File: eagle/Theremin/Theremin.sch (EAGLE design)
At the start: 82 parts, among them Q1 2N3904, Q2 2N3904, Q3 2N3904, Q4 2N3904, Q6 2N3904, Q7 2N3904, Q8 2N3904, U1 LM78L12, U2 LM79L12

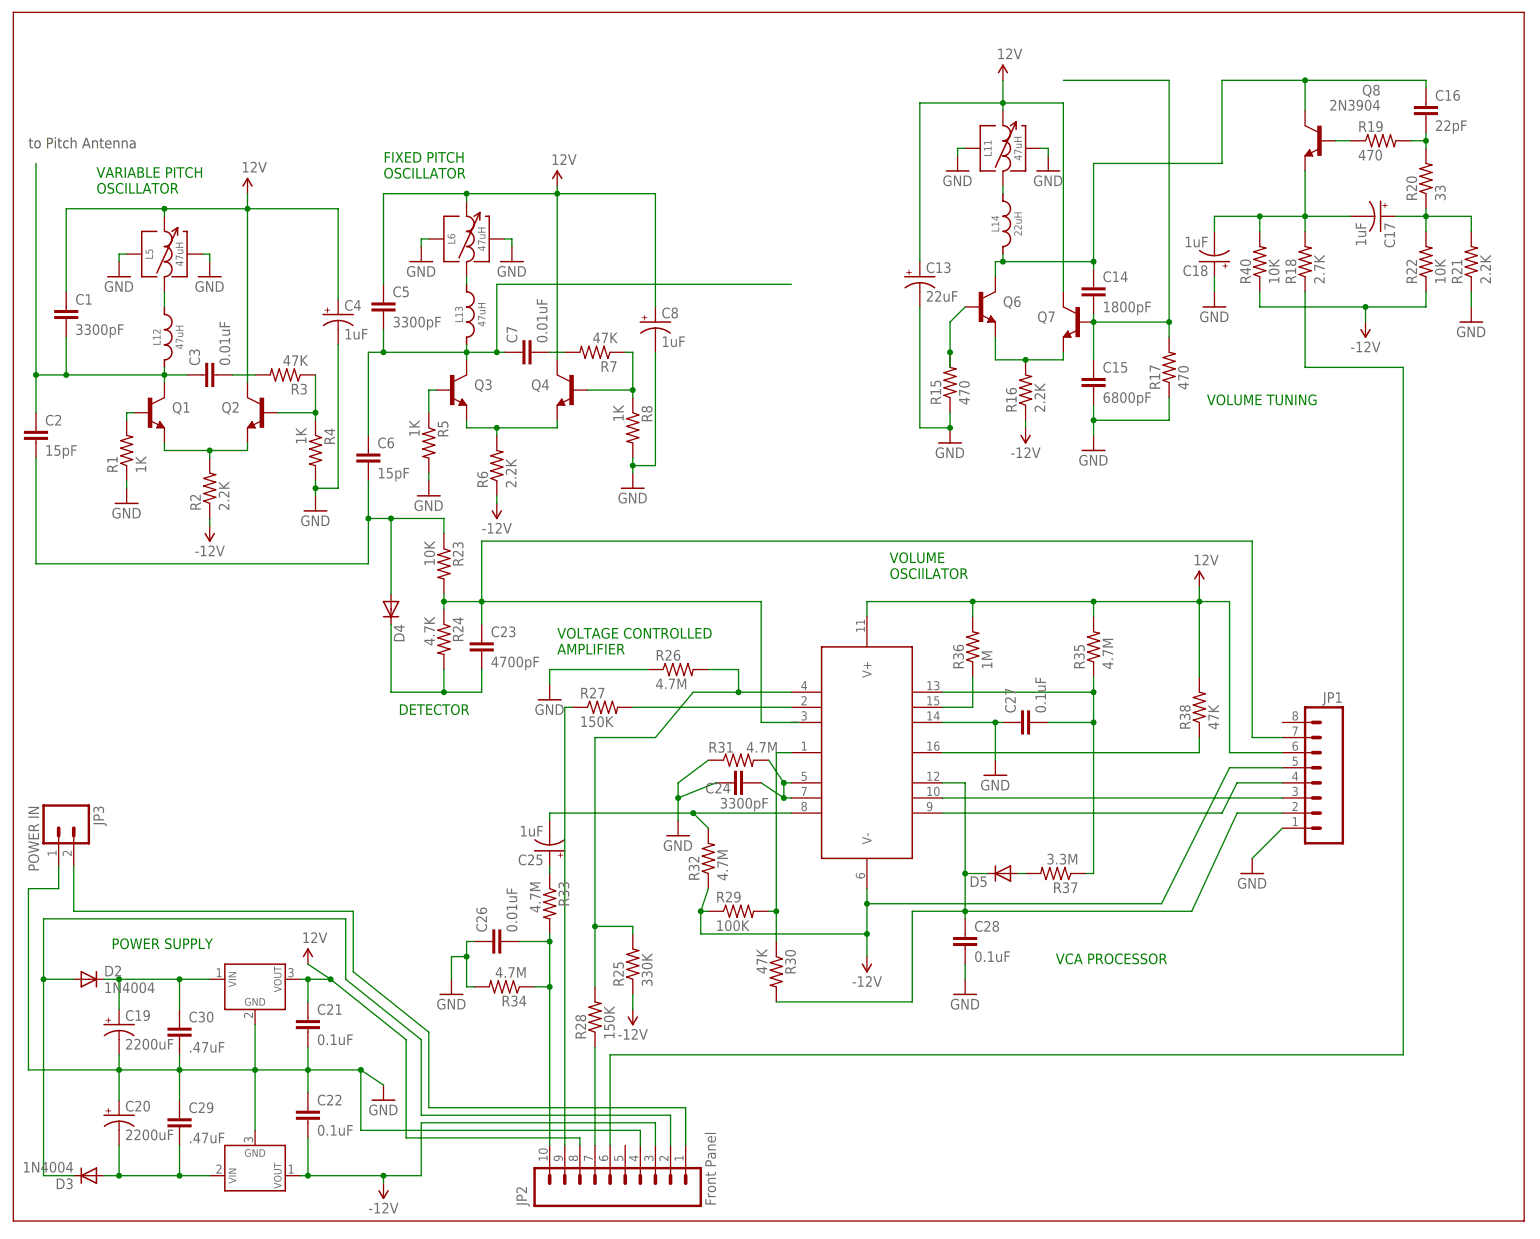
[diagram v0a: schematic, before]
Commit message: Add PITCH TUNING curcuit
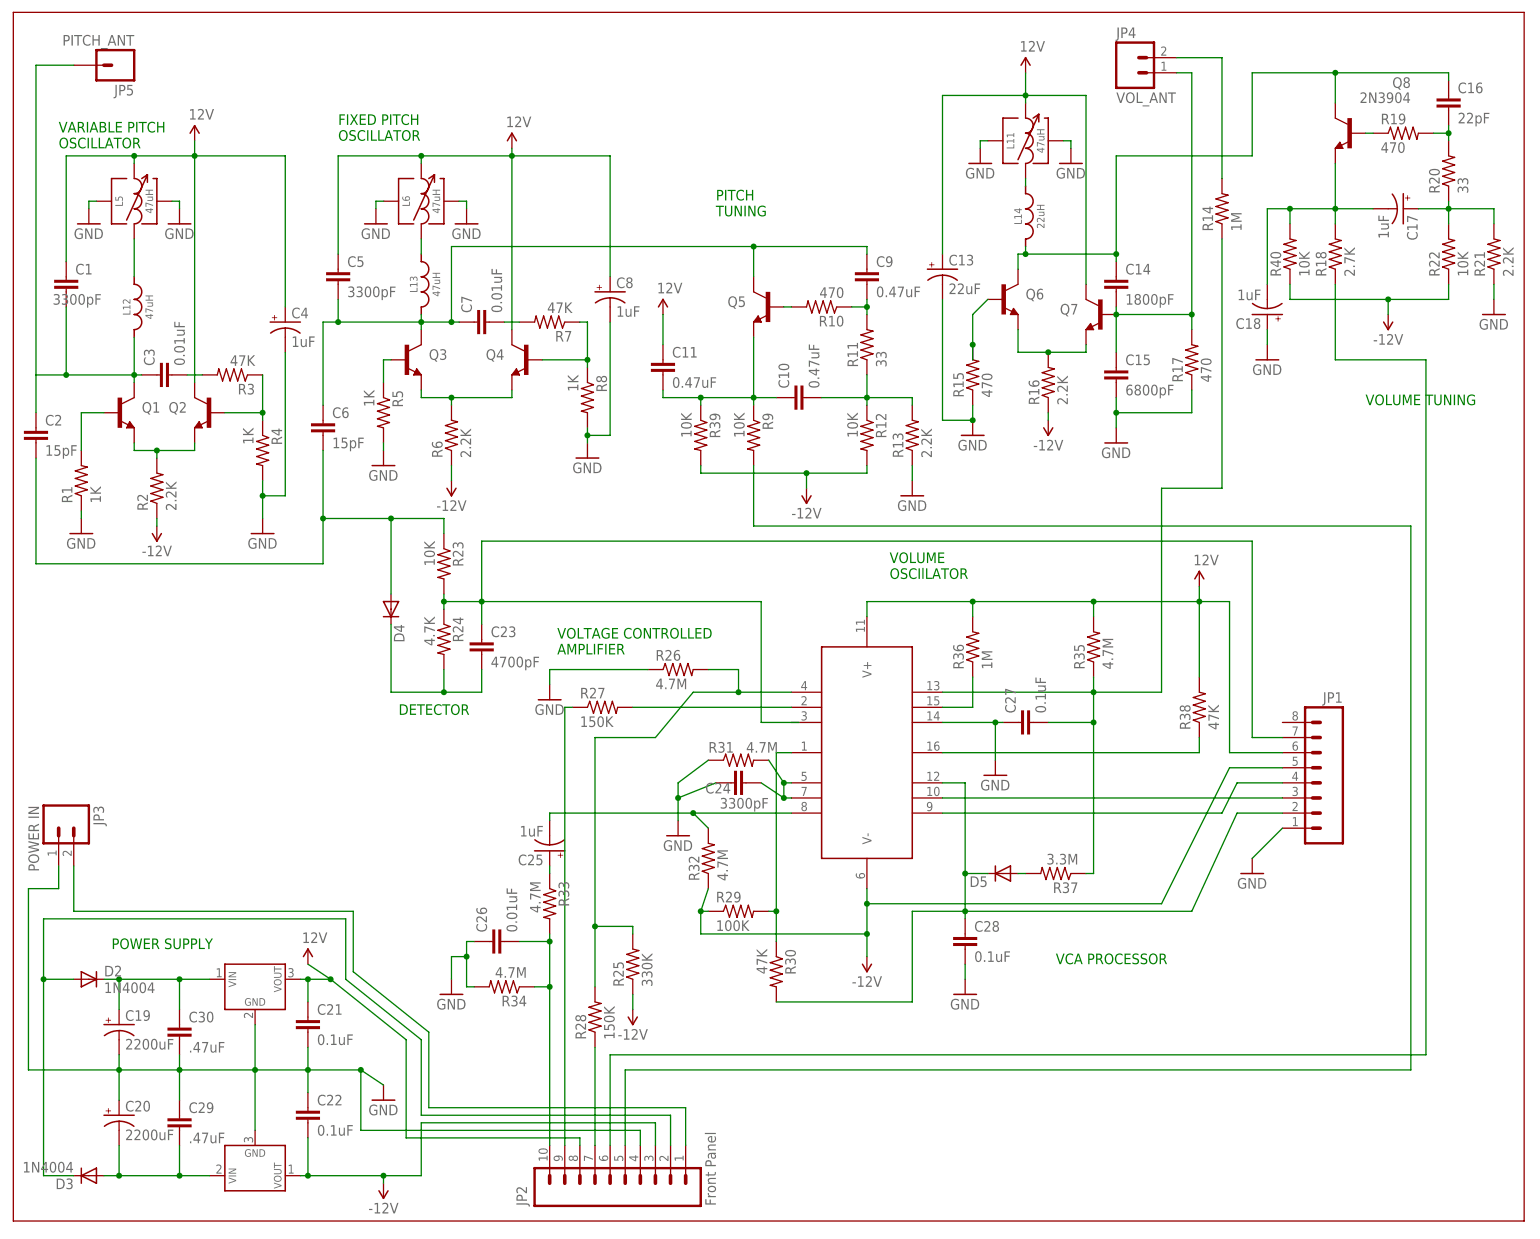
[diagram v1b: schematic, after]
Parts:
- added C10, C11, C9: 0.47uF, SparkFun-Capacitors:CAPPTH1
- added JP4: VOL_ANT, SparkFun-Connectors:M02LOCK_LONGPADS
- added JP5: PITCH_ANT, SparkFun-Connectors:M01PTH_LONGPAD
- added Q5: 2N3904, transistor:2N3904
- added R10: 470, SparkFun-Passives:RESISTOREZ
- added R11: 33, SparkFun-Passives:RESISTOREZ
- added R12, R39, R9: 10K, SparkFun-Resistors:RESISTORPTH-1/4W
- added R13: 2.2K, SparkFun-Passives:RESISTOREZ
- added R14: 1M, SparkFun-Passives:RESISTOREZ
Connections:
- new net N$15: JP4.2, R14.2
- new net N$45: C10.1, C11.2, Q5.E, R39.1, R9.1
- new net N$47: JP2.5, R9.2
- new net N$49: Q5.B, R10.2
- new net N$50: C9.2, R10.1, R11.2
- new net N$51: C10.2, R11.1, R12.1, R13.2
- net 5V: now also C11.1
- net GND: now also R13.1
- net N$17: now also JP5.1
- net N$26: now also R14.1
- net N$41: now also C9.1, Q5.C
- net N$9: now also JP4.1
- net VNEG: now also R12.2, R39.2
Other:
- note added: "PITCH TUNING"
- note removed: "to Pitch Antenna"
- moved on the sheet: C1, C13, C14, C15, C16, C17, C18, C3, C4, C5, C6, C7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

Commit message: Add jumper and resistor for selecting output amp type
Normal (keyboard, stereo) and Guitar / Bass
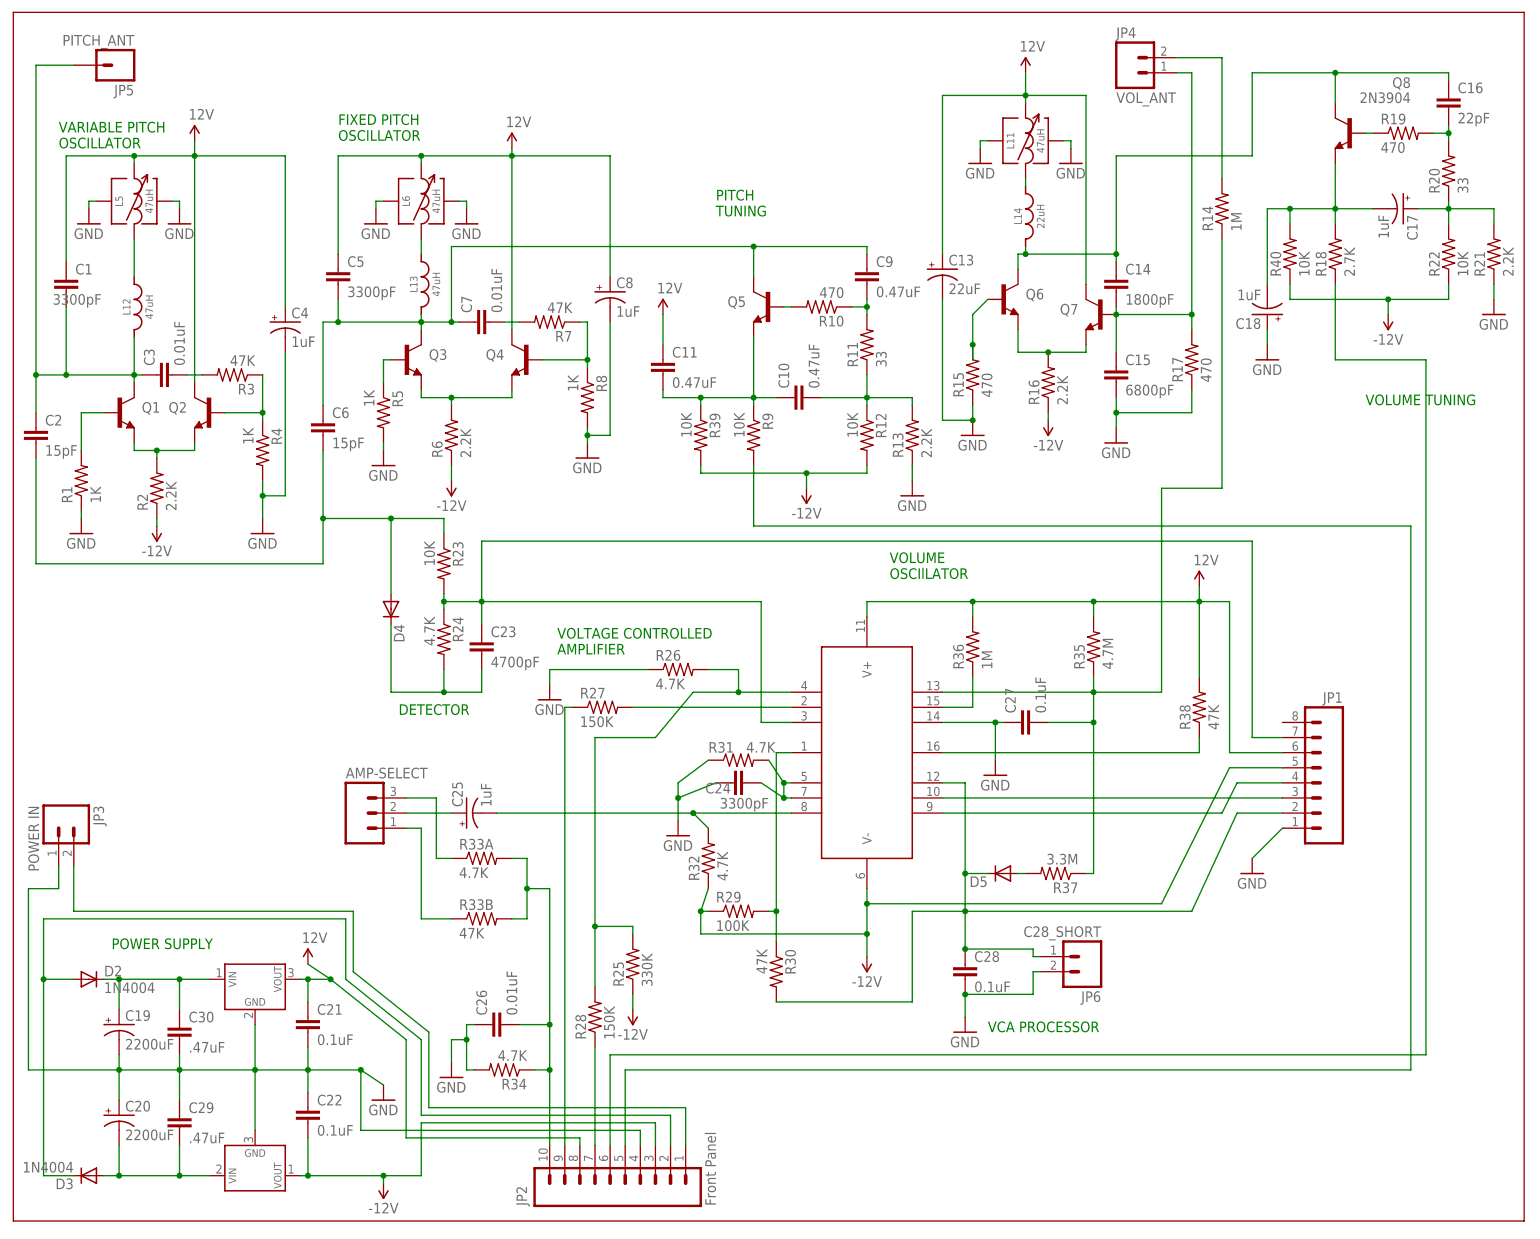
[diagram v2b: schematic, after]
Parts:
- removed R33: 4.7M, SparkFun-Passives:RESISTOREZ
- added AMP-SELECT: (no value), SparkFun-Connectors:M03LOCK_LONGPADS
- added JP6: C28_SHORT, SparkFun-Connectors:M02LOCK
- added R33A: 4.7K, SparkFun-Passives:RESISTOREZ
- added R33B: 47K, SparkFun-Passives:RESISTOREZ
- R26, R31, R32, R34: value 4.7M -> 4.7K
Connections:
- removed net N$31: C26.2, JP2.10, R33.2, R34.1
- new net N$52: AMP-SELECT.3, R33A.1
- new net N$53: AMP-SELECT.1, R33B.1
- new net N$54: C26.2, JP2.10, R33A.2, R33B.2, R34.1
- net GND: now also JP6.2
- net N$24: now also JP6.1
- net N$30: now also AMP-SELECT.2; no longer R33.1
- net N$37: now also U3.IN-PLUS-A
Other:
- moved on the sheet: C25, C26, C28, R34

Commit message: Clean up board layout
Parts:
- R10, R11, R13, R14, R15, R16, R17, R18, R19, R20, R21, R22, R26, R31, R32, R33A, R33B, R34, R35, R36, R37, R38, R40: device SparkFun-Passives:RESISTOREZ -> SparkFun-Resistors:RESISTORPTH-1/4W
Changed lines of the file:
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@@
 <setting verticaltext="up"/>
 </settings>
-<grid distance="0.05" unitdist="inch" unit="inch" style="lines" multiple="1" display="yes" altdistance="0.01" altunitdist="inch" altunit="inch"/>
+<grid distance="0.1" unitdist="inch" unit="inch" style="lines" multiple="1" display="no" altdistance="0.01" altunitdist="inch" altunit="inch"/>
 <layers>
 <layer number="1" name="Top" color="4" fill="1" visible="no" active="no"/>
@@
 <parts>
 <part name="Q8" library="transistor" deviceset="2N3904" device=""/>
-<part name="R19" library="SparkFun-Passives" deviceset="RESISTOR" device="EZ" value="470"/>
-<part name="R15" library="SparkFun-Passives" deviceset="RESISTOR" device="EZ" value="470"/>
-<part name="R17" library="SparkFun-Passives" deviceset="RESISTOR" device="EZ" value="470"/>
-<part name="R18" library="SparkFun-Passives" deviceset="RESISTOR" device="EZ" value="2.7K"/>
-<part name="R20" library="SparkFun-Passives" deviceset="RESISTOR" device="EZ" value="33"/>
+<part name="R19" library="SparkFun-Resistors" deviceset="RESISTOR" device="PTH-1/4W" value="470"/>
+<part name="R15" library="SparkFun-Resistors" deviceset="RESISTOR" device="PTH-1/4W" value="470"/>
+<part name="R17" library="SparkFun-Resistors" deviceset="RESISTOR" device="PTH-1/4W" value="470"/>
+<part name="R18" library="SparkFun-Resistors" deviceset="RESISTOR" device="PTH-1/4W" value="2.7K"/>
+<part name="R20" library="SparkFun-Resistors" deviceset="RESISTOR" device="PTH-1/4W" value="33"/>
 <part name="C17" library="SparkFun-Passives" deviceset="CAP_POL" device="PTH2" value="1uF"/>
 <part name="C18" library="SparkFun-Passives" deviceset="CAP_POL" device="PTH2" value="1uF"/>
 <part name="C16" library="SparkFun-Passives" deviceset="CAP" device="EZ" value="22pF"/>
-<part name="R22" library="SparkFun-Passives" deviceset="RESISTOR" device="EZ" value="10K"/>
-<part name="R21" library="SparkFun-Passives" deviceset="RESISTOR" device="EZ" value="2.2K"/>
+<part name="R22" library="SparkFun-Resistors" deviceset="RESISTOR" device="PTH-1/4W" value="10K"/>
+<part name="R21" library="SparkFun-Resistors" deviceset="RESISTOR" device="PTH-1/4W" value="2.2K"/>
 <part name="GND1" library="supply1" deviceset="GND" device=""/>
-<part name="R40" library="SparkFun-Passives" deviceset="RESISTOR" device="EZ" value="10K"/>
+<part name="R40" library="SparkFun-Resistors" deviceset="RESISTOR" device="PTH-1/4W" value="10K"/>
 <part name="GND2" library="supply1" deviceset="GND" device=""/>
 <part name="P-1" library="SparkFun-Aesthetics" deviceset="VNEG" device="" value="-12V"/>
 <part name="Q7" library="transistor" deviceset="2N3904" device="" value=""/>
 <part name="Q6" library="transistor" deviceset="2N3904" device="" value=""/>
-<part name="R16" library="SparkFun-Passives" deviceset="RESISTOR" device="EZ" value="2.2K"/>
+<part name="R16" library="SparkFun-Resistors" deviceset="RESISTOR" device="PTH-1/4W" value="2.2K"/>
 <part name="P-3" library="SparkFun-Aesthetics" deviceset="VNEG" device="" value="-12V"/>
 <part name="GND3" library="supply1" deviceset="GND" device=""/>
@@
 <part name="JP1" library="SparkFun-Connectors" deviceset="M08" device="1X08"/>
 <part name="GND12" library="supply1" deviceset="GND" device=""/>
-<part name="R38" library="SparkFun-Passives" deviceset="RESISTOR" device="EZ" value="47K"/>
+<part name="R38" library="SparkFun-Resistors" deviceset="RESISTOR" device="PTH-1/4W" value="47K"/>
 <part name="SUPPLY3" library="SparkFun-Aesthetics" deviceset="5V" device="" value="12V"/>
 <part name="P-4" library="SparkFun-Aesthetics" deviceset="VNEG" device="" value="-12V"/>
@@
 <part name="C28" library="SparkFun-Capacitors" deviceset="CAP" device="PTH" value="0.1uF"/>
 <part name="D5" library="SparkFun-DiscreteSemi" deviceset="DIODE" device="1N4148"/>
-<part name="R37" library="SparkFun-Passives" deviceset="RESISTOR" device="EZ" value="3.3M"/>
+<part name="R37" library="SparkFun-Resistors" deviceset="RESISTOR" device="PTH-1/4W" value="3.3M"/>
 <part name="C27" library="SparkFun-Capacitors" deviceset="CAP" device="PTH" value="0.1uF"/>
 <part name="GND14" library="supply1" deviceset="GND" device=""/>
-<part name="R36" library="SparkFun-Passives" deviceset="RESISTOR" device="EZ" value="1M"/>
-<part name="R35" library="SparkFun-Passives" deviceset="RESISTOR" device="EZ" value="4.7M"/>
+<part name="R36" library="SparkFun-Resistors" deviceset="RESISTOR" device="PTH-1/4W" value="1M"/>
+<part name="R35" library="SparkFun-Resistors" deviceset="RESISTOR" device="PTH-1/4W" value="4.7M"/>
 <part name="JP2" library="SparkFun-Connectors" deviceset="M10" device="LOCK_LONGPADS" value="Front Panel"/>
 <part name="R30" library="SparkFun-Resistors" deviceset="RESISTOR" device="PTH-1/4W" value="47K"/>
 <part name="R29" library="SparkFun-Resistors" deviceset="RESISTOR" device="PTH-1/4W" value="100K"/>
-<part name="R32" library="SparkFun-Passives" deviceset="RESISTOR" device="EZ" value="4.7K"/>
+<part name="R32" library="SparkFun-Resistors" deviceset="RESISTOR" device="PTH-1/4W" value="4.7K"/>
 <part name="C25" library="SparkFun-Passives" deviceset="CAP_POL" device="PTH2" value="1uF"/>
-<part name="R33A" library="SparkFun-Passives" deviceset="RESISTOR" device="EZ" value="4.7K"/>
+<part name="R33A" library="SparkFun-Resistors" deviceset="RESISTOR" device="PTH-1/4W" value="4.7K"/>
 <part name="C26" library="marky-parts" deviceset="CAP-5M-RADIAL" device="" value="0.01uF"/>
-<part name="R34" library="SparkFun-Passives" deviceset="RESISTOR" device="EZ" value="4.7K"/>
+<part name="R34" library="SparkFun-Resistors" deviceset="RESISTOR" device="PTH-1/4W" value="4.7K"/>
 <part name="GND16" library="supply1" deviceset="GND" device=""/>
 <part name="C24" library="SparkFun-Capacitors" deviceset="CAP" device="PTH" value="3300pF"/>
-<part name="R31" library="SparkFun-Passives" deviceset="RESISTOR" device="EZ" value="4.7K"/>
+<part name="R31" library="SparkFun-Resistors" deviceset="RESISTOR" device="PTH-1/4W" value="4.7K"/>
 <part name="GND17" library="supply1" deviceset="GND" device=""/>
 <part name="R28" library="SparkFun-Resistors" deviceset="RESISTOR" device="PTH-1/4W" value="150K"/>
-<part name="R26" library="SparkFun-Passives" deviceset="RESISTOR" device="EZ" value="4.7K"/>
+<part name="R26" library="SparkFun-Resistors" deviceset="RESISTOR" device="PTH-1/4W" value="4.7K"/>
 <part name="GND18" library="supply1" deviceset="GND" device=""/>
 <part name="P-6" library="SparkFun-Aesthetics" deviceset="VNEG" device="" value="-12V"/>
@@
 <part name="R39" library="SparkFun-Resistors" deviceset="RESISTOR" device="PTH-1/4W" value="10K"/>
 <part name="R9" library="SparkFun-Resistors" deviceset="RESISTOR" device="PTH-1/4W" value="10K"/>
-<part name="R10" library="SparkFun-Passives" deviceset="RESISTOR" device="EZ" value="470"/>
-<part name="R11" library="SparkFun-Passives" deviceset="RESISTOR" device="EZ" value="33"/>
+<part name="R10" library="SparkFun-Resistors" deviceset="RESISTOR" device="PTH-1/4W" value="470"/>
+<part name="R11" library="SparkFun-Resistors" deviceset="RESISTOR" device="PTH-1/4W" value="33"/>
 <part name="R12" library="SparkFun-Resistors" deviceset="RESISTOR" device="PTH-1/4W" value="10K"/>
-<part name="R13" library="SparkFun-Passives" deviceset="RESISTOR" device="EZ" value="2.2K"/>
+<part name="R13" library="SparkFun-Resistors" deviceset="RESISTOR" device="PTH-1/4W" value="2.2K"/>
 <part name="GND22" library="supply1" deviceset="GND" device=""/>
 <part name="C10" library="SparkFun-Capacitors" deviceset="CAP" device="PTH1" value="0.47uF"/>
@@
 <part name="JP4" library="SparkFun-Connectors" deviceset="M02" device="LOCK_LONGPADS" value="VOL_ANT"/>
 <part name="JP5" library="SparkFun-Connectors" deviceset="M01" device="PTH_LONGPAD" value="PITCH_ANT"/>
-<part name="R14" library="SparkFun-Passives" deviceset="RESISTOR" device="EZ" value="1M"/>
+<part name="R14" library="SparkFun-Resistors" deviceset="RESISTOR" device="PTH-1/4W" value="1M"/>
 <part name="JP6" library="SparkFun-Connectors" deviceset="M02" device="LOCK" value="C28_SHORT"/>
-<part name="R33B" library="SparkFun-Passives" deviceset="RESISTOR" device="EZ" value="47K"/>
+<part name="R33B" library="SparkFun-Resistors" deviceset="RESISTOR" device="PTH-1/4W" value="47K"/>
 <part name="AMP-SELECT" library="SparkFun-Connectors" deviceset="M03" device="LOCK_LONGPADS"/>
 </parts>
